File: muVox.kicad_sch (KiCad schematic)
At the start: 57 parts, among them J1 STEMMA QT, J2 JTAG_EXTRA, J3 Programmer, J4 Alt.DC, J5 DC IN, SW1 EG120A, U1 TPS5430DDA, U2 ZD24C08AE1, U3 XC6220B331MR

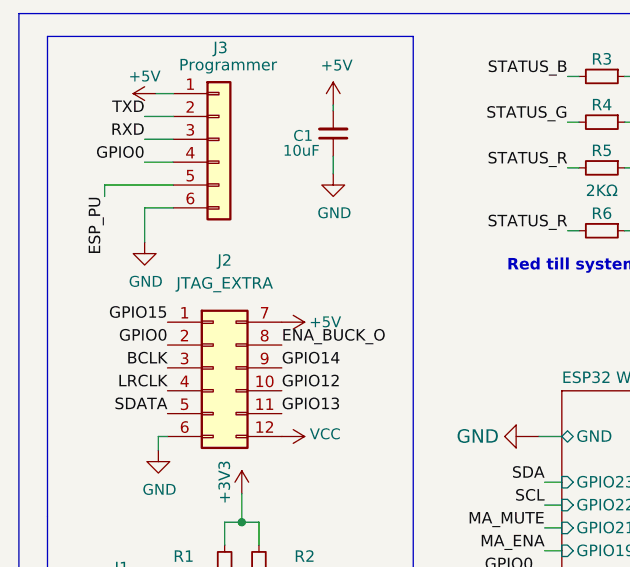
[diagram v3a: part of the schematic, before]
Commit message: Added missing partsnumbers and ordered latest rev. PCBS
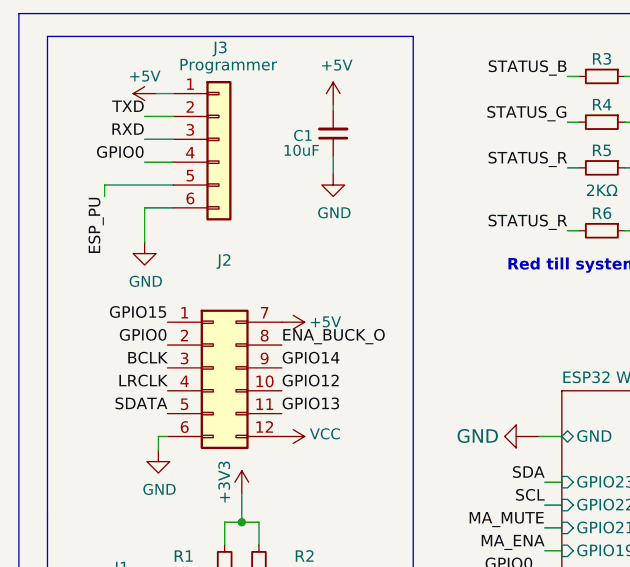
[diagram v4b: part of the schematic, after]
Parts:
- J2: value JTAG_EXTRA -> (none); footprint Connector_IDC:IDC-Header_2x06_P2.54mm_Vertical -> (none); LCSC (none) -> C601938
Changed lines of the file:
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@@
     (in_bom yes) (on_board yes) (fields_autoplaced)
     (property "Reference" "J2" (id 0) (at 57.531 51.943 0))
-    (property "Value" "JTAG_EXTRA" (id 1) (at 57.531 54.483 0))
-    (property "Footprint" "Connector_IDC:IDC-Header_2x06_P2.54mm_Vertical" (id 2) (at 56.261 63.881 0)
+    (property "Value" "" (id 1) (at 57.531 54.483 0))
+    (property "Footprint" "" (id 2) (at 56.261 63.881 0)
       (effects (font (size 1.27 1.27)) hide)
     )
     (property "Datasheet" "~" (id 3) (at 56.261 63.881 0)
+      (effects (font (size 1.27 1.27)) hide)
+    )
+    (property "LCSC" "C601938" (id 4) (at 56.261 63.881 0)
       (effects (font (size 1.27 1.27)) hide)
     )
@@
     )
     (path "/3ddaeb0a-149b-4c6d-a910-a2d3377e0f7c/2be21e64-157c-48c0-a548-c7a70387c480"
-      (reference "C8") (unit 1) (value "22uF") (footprint "Capacitor_SMD:C_0603_1608Metric")
+      (reference "C8") (unit 1) (value "22nF") (footprint "Capacitor_SMD:C_0603_1608Metric")
     )
     (path "/3ddaeb0a-149b-4c6d-a910-a2d3377e0f7c/00000000-0000-0000-0000-000060735859"

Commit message: Minor changes. Flipped Q2 PMOS and fixed some silkscreening
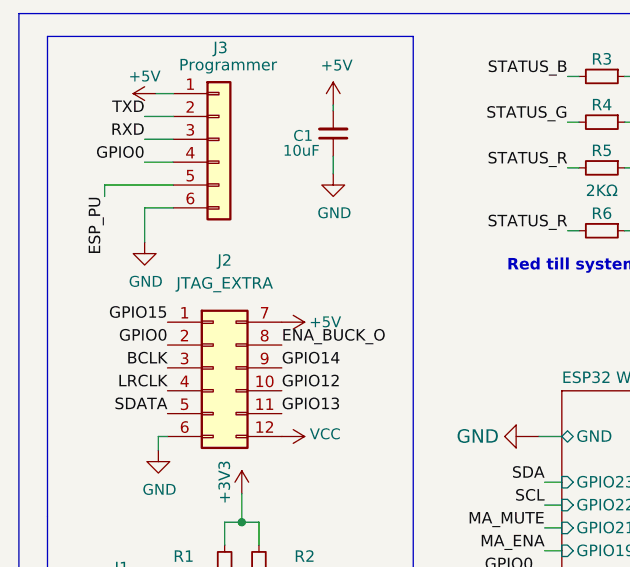
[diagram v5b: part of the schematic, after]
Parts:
- J2: value (none) -> JTAG_EXTRA; footprint (none) -> Connector_IDC:IDC-Header_2x06_P2.54mm_Vertical
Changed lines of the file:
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@@
     (in_bom yes) (on_board yes) (fields_autoplaced)
     (property "Reference" "J2" (id 0) (at 57.531 51.943 0))
-    (property "Value" "" (id 1) (at 57.531 54.483 0))
-    (property "Footprint" "" (id 2) (at 56.261 63.881 0)
+    (property "Value" "JTAG_EXTRA" (id 1) (at 57.531 54.483 0))
+    (property "Footprint" "Connector_IDC:IDC-Header_2x06_P2.54mm_Vertical" (id 2) (at 56.261 63.881 0)
       (effects (font (size 1.27 1.27)) hide)
     )

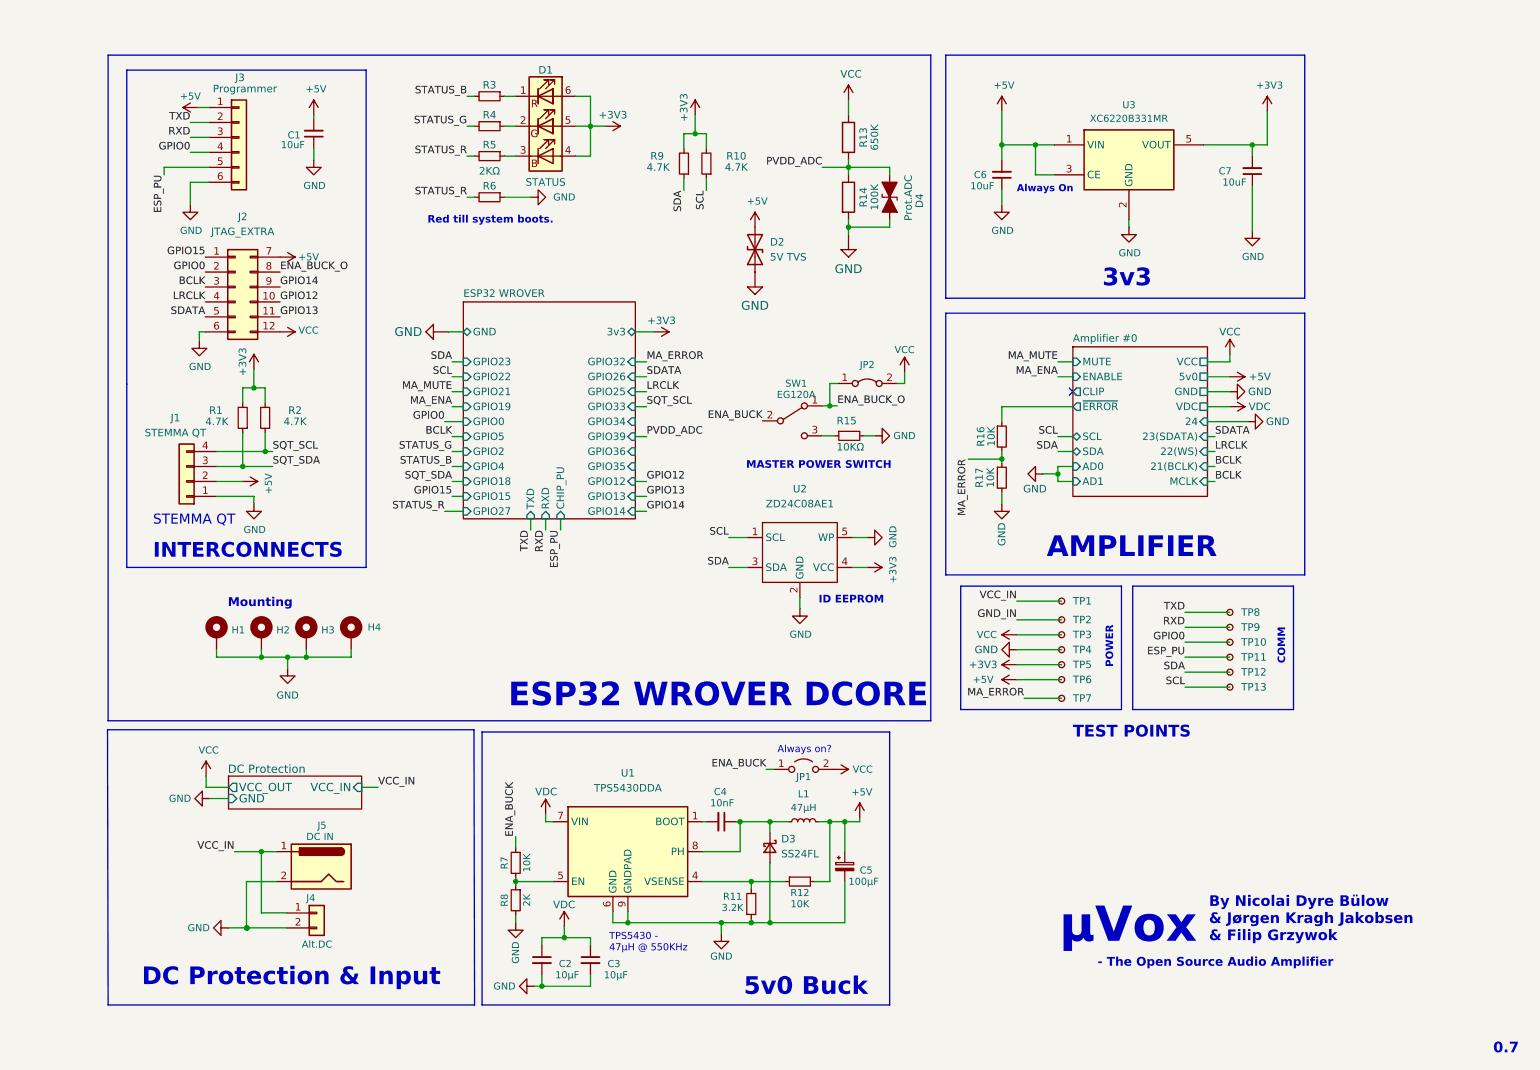
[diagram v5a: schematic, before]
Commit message: Updated all schematic values and parts numbers
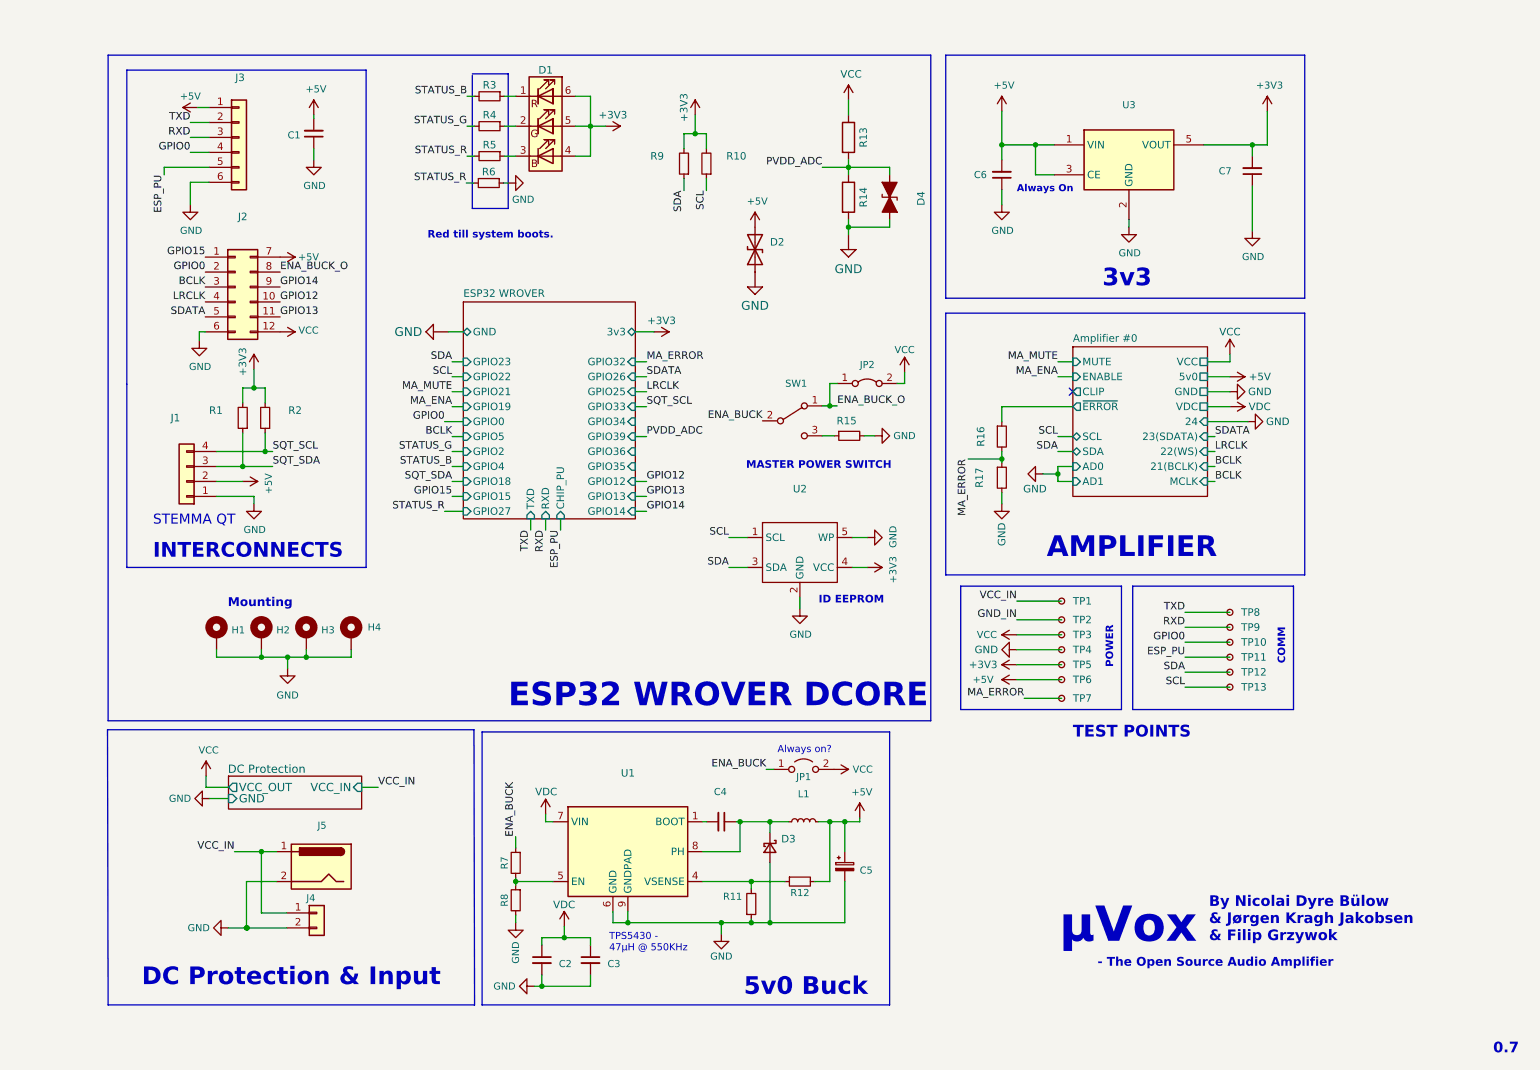
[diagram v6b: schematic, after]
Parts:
- C1: value 10uF -> (none); footprint Capacitor_SMD:C_0805_2012Metric -> (none)
- C2, C3: value 10µF -> (none); footprint Capacitor_SMD:C_0805_2012Metric -> (none)
- C4: value 10nF -> (none); footprint Capacitor_SMD:C_0805_2012Metric -> (none)
- C5: value 100µF -> (none); footprint Capacitor_SMD:C_Elec_5x5.4 -> (none)
- C6, C7: value 10uF -> (none); footprint Capacitor_SMD:C_0805_2012Metric -> (none); LCSC C519978 -> C15850
- D1: value STATUS -> (none); footprint LED_SMD:LED_WS2812_PLCC6_5.0x5.0mm_P1.6mm -> (none); Distributor TME -> (none); Identifier FYLS-5050NRGBC -> (none); TME (none) -> FYLS-5050NRGBC
- D2: value 5V TVS -> (none); footprint Diode_SMD:D_SOD-323 -> (none)
- D3: value SS24FL -> (none); footprint Diode_SMD:D_SOD-123F -> (none)
- D4: value Prot.ADC -> (none); footprint Diode_SMD:D_SOD-323 -> (none)
- H1, H2, H3, H4: value MountingHole_Pad -> (none); footprint Lib:MountingHole_PSUDO_M4 -> (none)
- J1: value STEMMA QT -> (none); footprint Connector_JST:JST_SH_SM04B-SRSS-TB_1x04-1MP_P1.00mm_Horizontal -> (none)
- J2: value JTAG_EXTRA -> (none); footprint Connector_IDC:IDC-Header_2x06_P2.54mm_Vertical -> (none)
- J3: value Programmer -> (none); footprint Connector_PinHeader_2.54mm:PinHeader_1x06_P2.54mm_Vertical -> (none); LCSC (none) -> C37208
- J4: value Alt.DC -> (none); footprint Connector_JST:JST_VH_B2PS-VH_1x02_P3.96mm_Horizontal -> (none); Digikey (none) -> 277-16667-ND
- J5: value DC IN -> (none); footprint Connector_BarrelJack:BarrelJack_CUI_PJ-063AH_Horizontal -> (none)
- JP1: value Jumper_2_Open -> (none); footprint Jumper:SolderJumper-2_P1.3mm_Open_RoundedPad1.0x1.5mm -> (none)
- JP2: value Jumper_2_Bridged -> (none); footprint Jumper:SolderJumper-2_P1.3mm_Bridged_RoundedPad1.0x1.5mm -> (none)
- L1: value 47µH -> (none); footprint Inductor_SMD:L_10.4x10.4_H4.8 -> (none)
- R1, R10, R2, R9: value 4.7K -> (none); footprint Resistor_SMD:R_0603_1608Metric -> (none); LCSC (none) -> C2907034
- R11: value 3.2K -> (none); footprint Resistor_SMD:R_0603_1608Metric -> (none)
- R12, R16, R17, R6, R7: value 10K -> (none); footprint Resistor_SMD:R_0603_1608Metric -> (none)
- R13: value 650K -> (none); footprint Resistor_SMD:R_0603_1608Metric -> (none)
- R14: value 100K -> (none); footprint Resistor_SMD:R_0603_1608Metric -> (none); LCSC C25803 -> C2906980
- R15: value 10KΩ -> (none); footprint Resistor_SMD:R_0603_1608Metric -> (none)
- R3, R4: value 800R -> (none); footprint Resistor_SMD:R_0603_1608Metric -> (none); LCSC (none) -> C2907022
- R5: value 2KΩ -> (none); footprint Resistor_SMD:R_0603_1608Metric -> (none); LCSC (none) -> C2907022
- R8: value 2K -> (none); footprint Resistor_SMD:R_0603_1608Metric -> (none)
- SW1: value EG120A -> (none); footprint Lib:SLIDE-SWITCH -> (none); Distributor TME -> (none)
- TP1, TP10, TP11, TP12, TP13, TP2, TP3, TP4, TP5, TP6, TP7, TP8, TP9: value TestPoint_Small -> (none); footprint TestPoint:TestPoint_Pad_D1.5mm -> (none)
- U1: value TPS5430DDA -> (none); footprint Package_SO:TI_SO-PowerPAD-8_ThermalVias -> (none)
- U2: value ZD24C08AE1 -> (none); footprint Package_TO_SOT_SMD:SOT-23-5 -> (none)
- U3: value XC6220B331MR -> (none); footprint Package_TO_SOT_SMD:SOT-23-5 -> (none)
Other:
- moved on the sheet: R6

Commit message: Updated revision nr on .sch
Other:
- note added: "0.9"
- note removed: "0.7"
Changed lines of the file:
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@@
     (effects (font (size 1.2954 1.2954) (thickness 0.2591) bold) (justify left bottom))
   )
-  (text "0.7" (at 269.875 194.31 0)
+  (text "0.9" (at 269.875 194.31 0)
     (effects (font (size 1.8034 1.8034) (thickness 0.3607) bold) (justify left bottom))
   )
